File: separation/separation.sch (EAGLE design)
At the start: 9 parts, among them IC1 L7805ACV

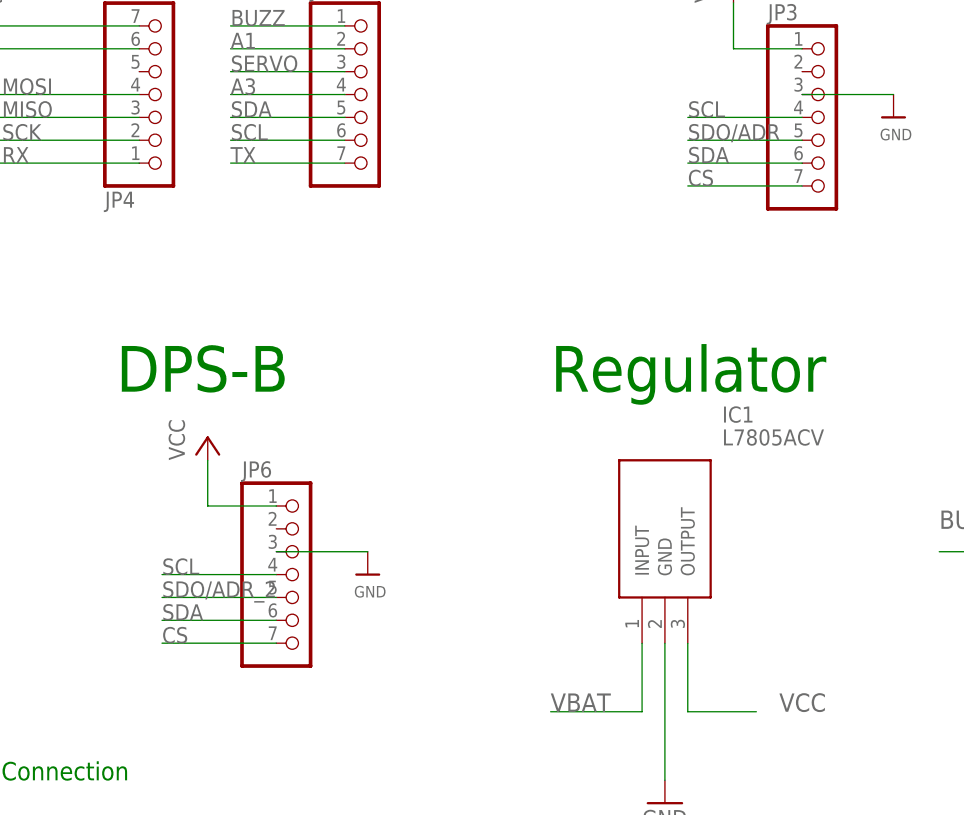
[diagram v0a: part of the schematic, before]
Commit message: remove cs lines
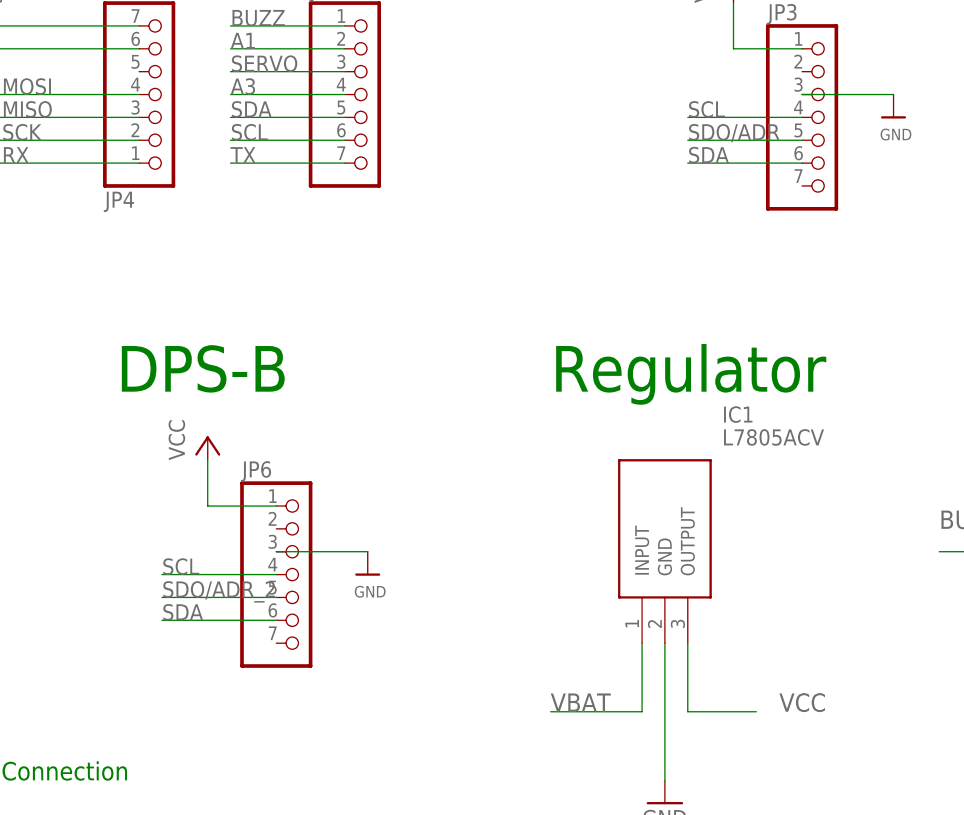
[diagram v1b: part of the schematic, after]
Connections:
- removed net CS: JP3.7, JP6.7
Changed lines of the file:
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@@
-</segment>
-</net>
-<net name="CS" class="0">
-<segment>
-<wire x1="106.68" y1="53.34" x2="93.98" y2="53.34" width="0.1524" layer="91"/>
-<label x="93.98" y="53.34" size="1.778" layer="95"/>
-<pinref part="JP3" gate="A" pin="7"/>
-</segment>
-<segment>
-<wire x1="48.26" y1="2.54" x2="35.56" y2="2.54" width="0.1524" layer="91"/>
-<label x="35.56" y="2.54" size="1.778" layer="95"/>
-<pinref part="JP6" gate="A" pin="7"/>
 </segment>
 </net>

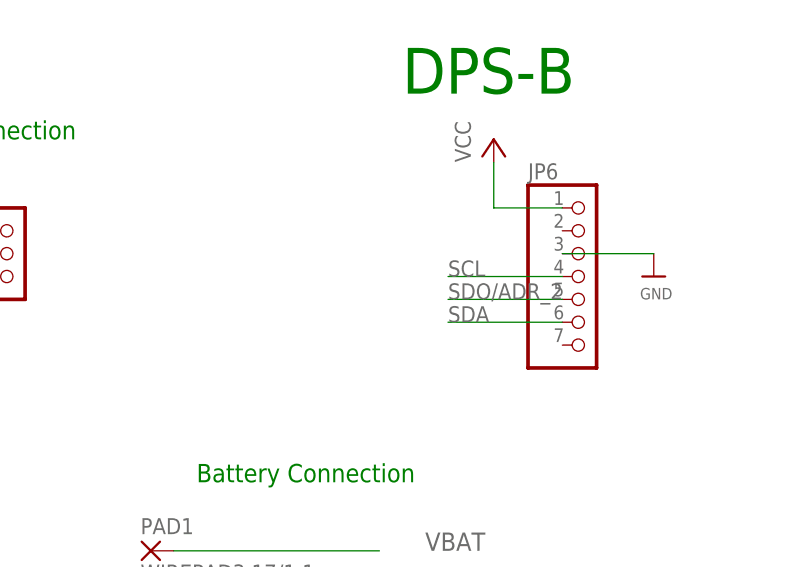
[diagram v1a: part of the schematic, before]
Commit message: tweak rp2040 tstop
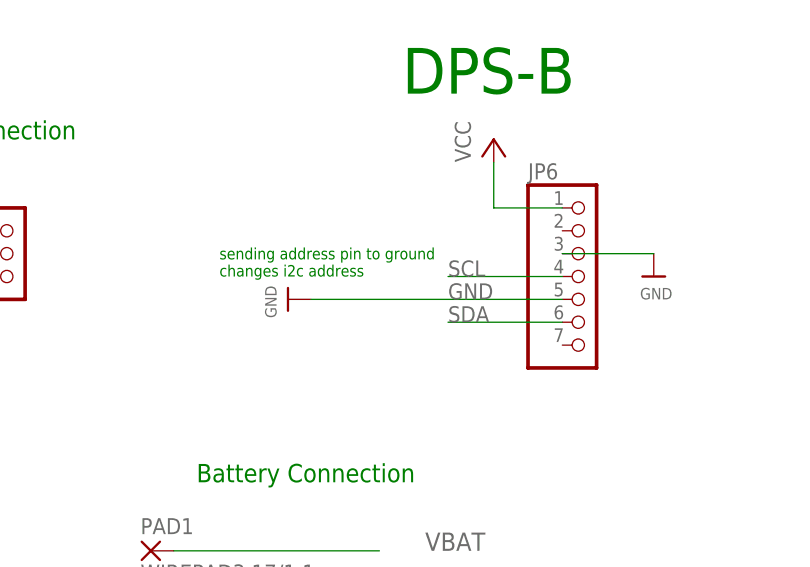
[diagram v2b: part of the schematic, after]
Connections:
- removed net SDO/ADR_2: JP6.5
- net GND: now also JP6.5
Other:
- note added: "sending address pin to ground changes i2c address"
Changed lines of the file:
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@@
 <part name="PAD2" library="wirepad" library_urn="urn:adsk.eagle:library:412" deviceset="WIREPAD" device="3,17/1,1" package3d_urn="urn:adsk.eagle:package:30832/1"/>
 <part name="U$4" library="microbuilder" deviceset="GND" device=""/>
+<part name="U$2" library="microbuilder" deviceset="GND" device=""/>
 </parts>
 <sheets>
@@
 <text x="-27.94" y="25.4" size="2.032" layer="91">Servo Connection</text>
 <text x="7.62" y="-12.7" size="2.032" layer="91">Battery Connection</text>
+<text x="10.16" y="10.16" size="1.27" layer="91">sending address pin to ground
+changes i2c address</text>
 </plain>
 <instances>
@@
 <attribute name="VALUE" x="27.94" y="-32.004" size="1.27" layer="96" rot="R90"/>
 </instance>
+<instance part="U$2" gate="G$1" x="17.78" y="7.62" smashed="yes" rot="R270">
+<attribute name="VALUE" x="15.24" y="9.144" size="1.27" layer="96" rot="R270"/>
+</instance>
 </instances>
 <busses>
@@
 <wire x1="5.08" y1="-30.48" x2="22.86" y2="-30.48" width="0.1524" layer="91"/>
 </segment>
+<segment>
+<label x="35.56" y="7.62" size="1.778" layer="95"/>
+<pinref part="JP6" gate="A" pin="5"/>
+<pinref part="U$2" gate="G$1" pin="GND"/>
+<wire x1="48.26" y1="7.62" x2="20.32" y2="7.62" width="0.1524" layer="91"/>
+</segment>
 </net>
 <net name="MOSI" class="0">
@@
 <label x="93.98" y="58.42" size="1.778" layer="95"/>
 <pinref part="JP3" gate="A" pin="5"/>
-</segment>
-</net>
-<net name="SDO/ADR_2" class="0">
-<segment>
-<wire x1="48.26" y1="7.62" x2="35.56" y2="7.62" width="0.1524" layer="91"/>
-<label x="35.56" y="7.62" size="1.778" layer="95"/>
-<pinref part="JP6" gate="A" pin="5"/>
 </segment>
 </net>
@@
 </drawing>
 <compatibility>
+<note version="6.3" minversion="6.2.2" severity="warning">
+Since Version 6.2.2 text objects can contain more than one line,
+which will not be processed correctly with this version.
+</note>
 <note version="8.2" severity="warning">
 Since Version 8.2, EAGLE supports online libraries. The ids
